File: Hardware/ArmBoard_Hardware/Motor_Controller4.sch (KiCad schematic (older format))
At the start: 13 parts

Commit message: added missing lables to connectors
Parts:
- MC4: symbol MRDT_ICs:VNH5019A_E -> ArmBoard_Hardware-rescue:VNH5019A_E-MRDT_ICs
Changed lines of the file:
@@
 IN_A_4
 $Comp
-L MRDT_ICs:VNH5019A_E U?
+L ArmBoard_Hardware-rescue:VNH5019A_E-MRDT_ICs U?
 U 1 1 62E6C81F
 P 4925 4600

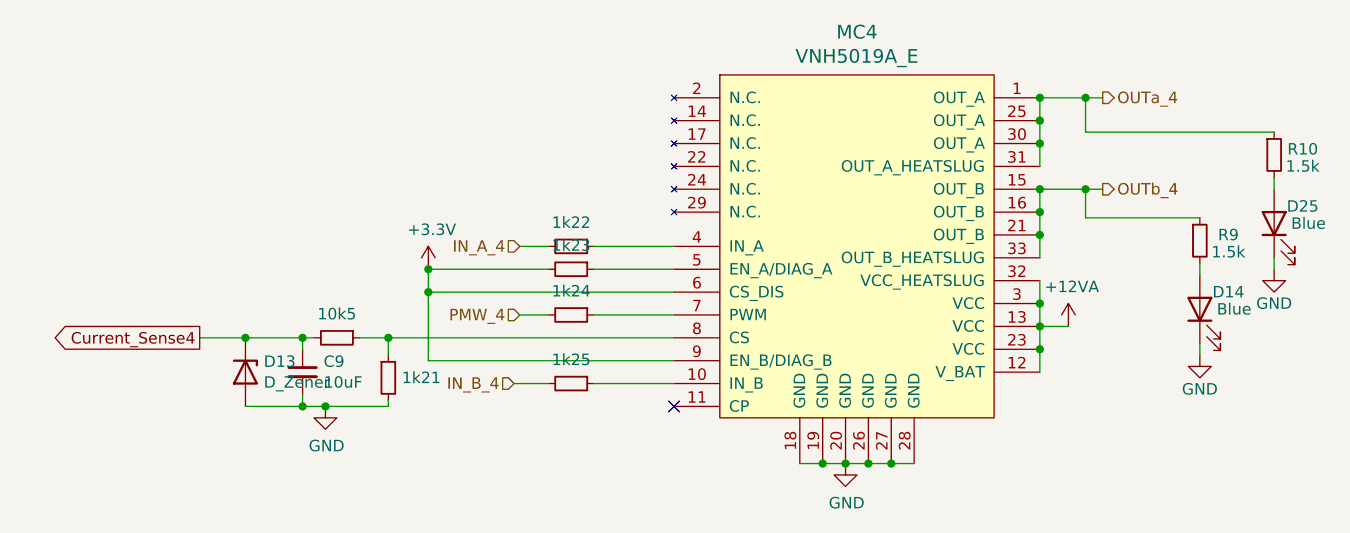
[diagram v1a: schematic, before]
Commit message: schematic changes, encoder changes, led changes
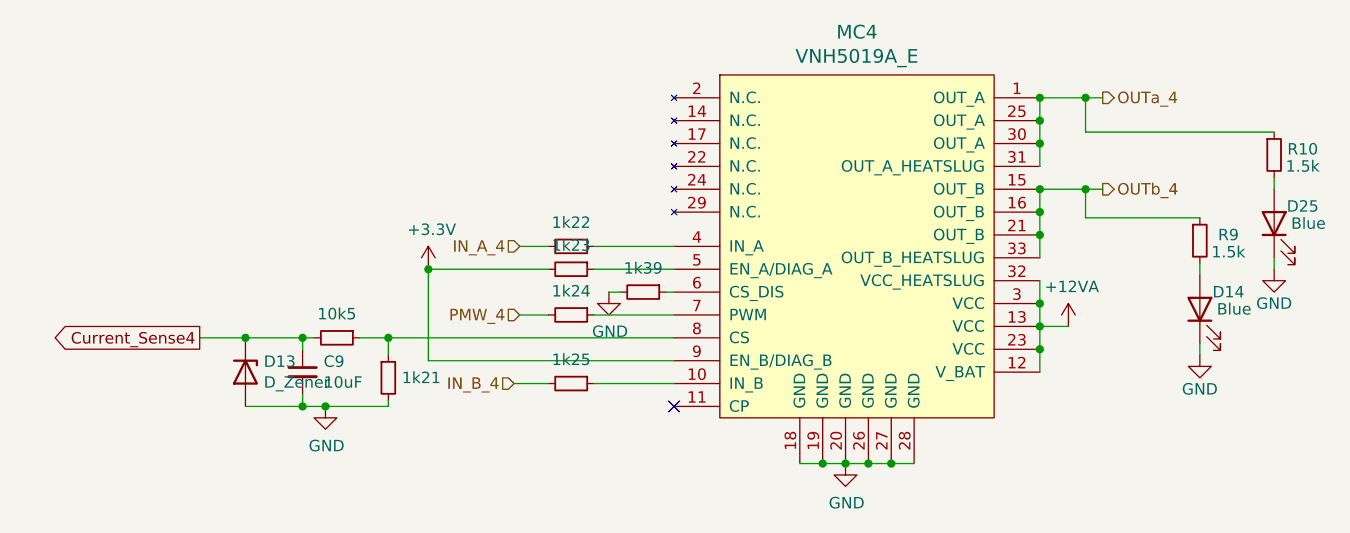
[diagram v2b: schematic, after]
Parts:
- added 1k39: R_Small, Resistor_SMD:R_0603_1608Metric_Pad0.98x0.95mm_HandSolder, symbol Device:R_Small
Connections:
- net +3V3: no longer MC4.6 (CS_DIS)
- net GND: now also 1k39.2
- new net: 1k39.1, MC4.6 (CS_DIS)
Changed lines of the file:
@@
 Wire Wire Line
 	4175 4150 4050 4150
-Wire Wire Line
-	4725 4050 3650 4050
-Wire Wire Line
-	3650 4050 3650 3950
 Connection ~ 3650 3950
 Wire Wire Line
 	4725 4350 3650 4350
-Wire Wire Line
-	3650 4350 3650 4050
-Connection ~ 3650 4050
 Wire Wire Line
 	4725 4250 3475 4250
@@
 Text HLabel 6600 3600 2    50   Output ~ 0
 OUTb_4
+Wire Wire Line
+	3650 3950 3650 4350
+$Comp
+L power:GND #PWR?
+U 1 1 62643622
+P 4440 4050
+AR Path="/63845F20/62643622" Ref="#PWR?"  Part="1"
+AR Path="/628CE14B/62643622" Ref="#PWR?"  Part="1"
+AR Path="/6297969A/62643622" Ref="#PWR?"  Part="1"
+AR Path="/629F46F6/62643622" Ref="#PWR?"  Part="1"
+AR Path="/629F46FD/62643622" Ref="#PWR?"  Part="1"
+AR Path="/62A5CC3B/62643622" Ref="#PWR?"  Part="1"
+AR Path="/62A5CC46/62643622" Ref="#PWR?"  Part="1"
+AR Path="/62AF9C52/62643622" Ref="#PWR?"  Part="1"
+AR Path="/62D2CE1B/62643622" Ref="#PWR06"  Part="1"
+F 0 "#PWR06" H 4440 3800 50  0001 C CNN
+F 1 "GND" H 4445 3877 50  0000 C CNN
+F 2 "" H 4440 4050 50  0001 C CNN
+F 3 "" H 4440 4050 50  0001 C CNN
+	1    4440 4050
+	1    0    0    -1
+$EndComp
+$Comp
+L Device:R_Small 1k?
+U 1 1 628AE51B
+P 4590 4050
+AR Path="/63845F20/628AE51B" Ref="1k?"  Part="1"
+AR Path="/628CE14B/628AE51B" Ref="1k?"  Part="1"
+AR Path="/6297969A/628AE51B" Ref="1k?"  Part="1"
+AR Path="/629F46F6/628AE51B" Ref="1k?"  Part="1"
+AR Path="/629F46FD/628AE51B" Ref="1k?"  Part="1"
+AR Path="/62A5CC3B/628AE51B" Ref="1k?"  Part="1"
+AR Path="/62A5CC46/628AE51B" Ref="1k?"  Part="1"
+AR Path="/62AF9C52/628AE51B" Ref="1k?"  Part="1"
+AR Path="/62C19165/628AE51B" Ref="1k?"  Part="1"
+AR Path="/62CA8FD7/628AE51B" Ref="1k?"  Part="1"
+AR Path="/62CBA1AC/628AE51B" Ref="1k?"  Part="1"
+AR Path="/62CCE879/628AE51B" Ref="1k?"  Part="1"
+AR Path="/62CE0B38/628AE51B" Ref="1k?"  Part="1"
+AR Path="/62CF1227/628AE51B" Ref="1k?"  Part="1"
+AR Path="/62D0C672/628AE51B" Ref="1k?"  Part="1"
+AR Path="/62D1BEB1/628AE51B" Ref="1k?"  Part="1"
+AR Path="/62D2CE1B/628AE51B" Ref="1k39"  Part="1"
+AR Path="/62D3BCB9/628AE51B" Ref="1k?"  Part="1"
+AR Path="/62D4BAA1/628AE51B" Ref="1k?"  Part="1"
+F 0 "1k39" V 4486 4050 50  0000 C CNN
+F 1 "R_Small" V 4485 4050 50  0001 C CNN
+F 2 "Resistor_SMD:R_0603_1608Metric_Pad0.98x0.95mm_HandSolder" H 4590 4050 50  0001 C CNN
+F 3 "~" H 4590 4050 50  0001 C CNN
+	1    4590 4050
+	0    1    1    0
+$EndComp
+Wire Wire Line
+	4440 4050 4490 4050
+Wire Wire Line
+	4690 4050 4725 4050
 $EndSCHEMATC

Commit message: gerbs added and zipped
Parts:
- MC4: symbol ArmBoard_Hardware-rescue:VNH5019A_E-MRDT_ICs -> MRDT_ICs:VNH5019A_E
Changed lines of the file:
@@
 IN_A_4
 $Comp
-L ArmBoard_Hardware-rescue:VNH5019A_E-MRDT_ICs U?
+L MRDT_ICs:VNH5019A_E U?
 U 1 1 62E6C81F
 P 4925 4600
